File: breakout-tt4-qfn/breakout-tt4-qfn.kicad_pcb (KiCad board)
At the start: 2 copper layers, 45 x 52.5 mm, 113 parts, among them U1 Caravel_QFN_TT4

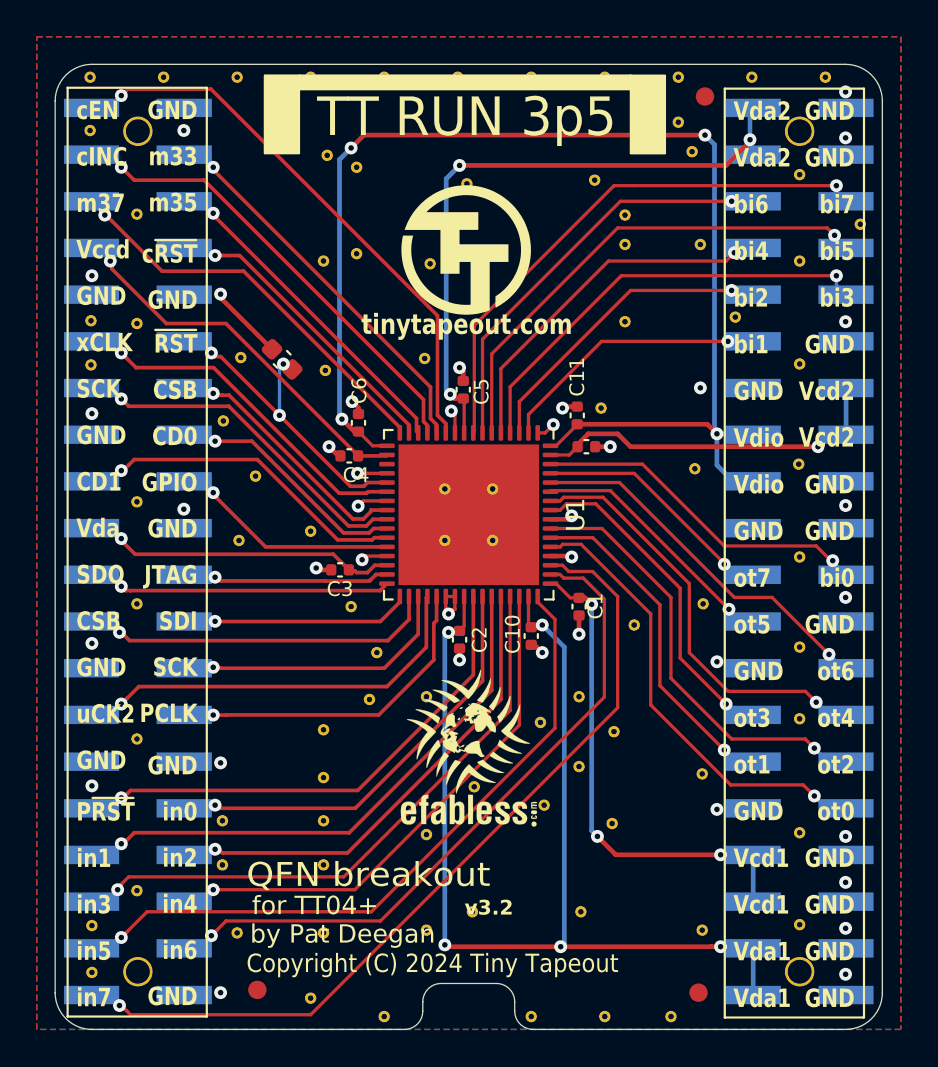
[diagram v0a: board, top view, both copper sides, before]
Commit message: modified silk for TT04
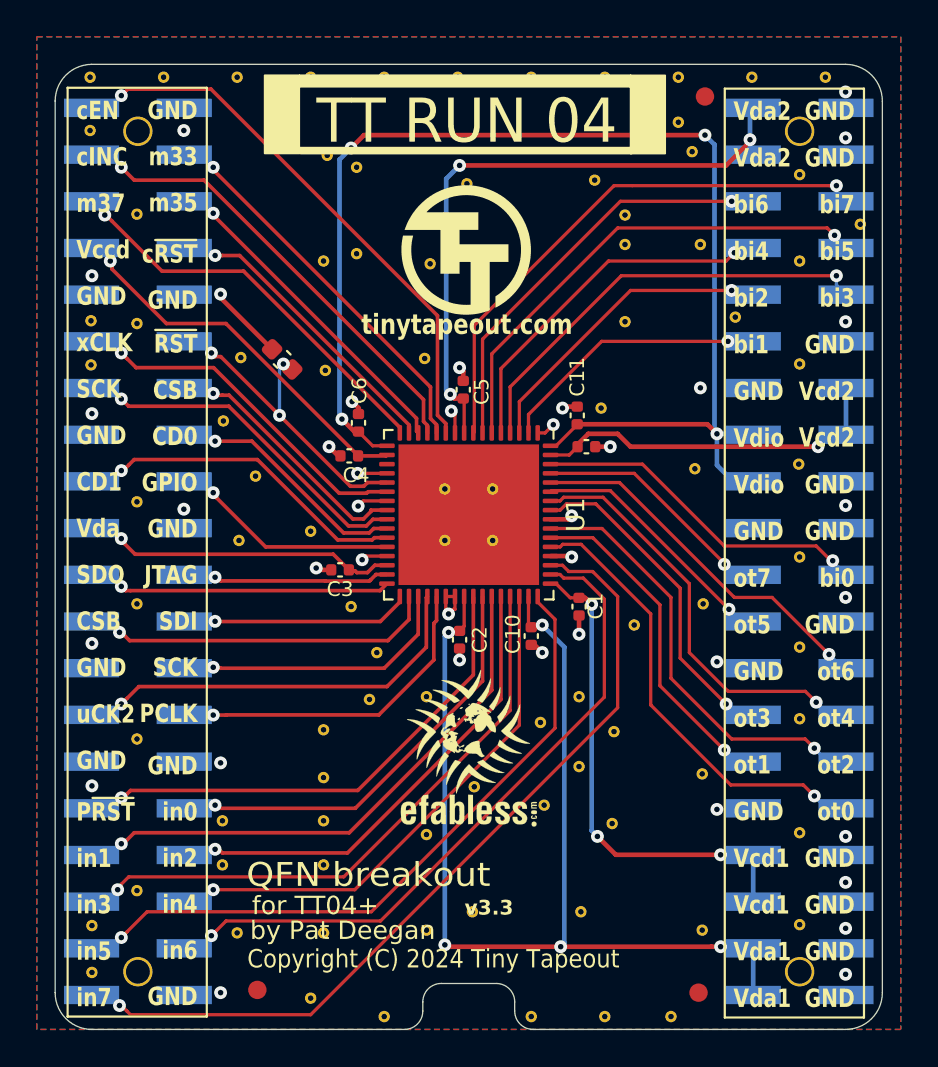
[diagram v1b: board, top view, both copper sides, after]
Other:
- board text added: "Design by Pat Deegan https://psychogenic.com"
- board text added: "TT RUN 04"
- board text added: "TinyTapeout designs are packaged together along with a MUX that allows for directing I/O to any selected project, controlled through the cINC, cEN and ~{cRST} pins. This PCB provides a way to deliver these chips that will sit atop the demo board, but also allows you to easily integrate the ICs into your own projects. For details, see"
- board text added: "github.com/TinyTapeout/breakout-pcb"
- board text added: "v3.3"
- board text removed: "TT RUN 3p5"
- board text removed: "TinyTapeout projects are packaged together within Caravel, an SoC that provides space for user projects, pads to connect to the outside world and other features like a microcontroller, logic analyzer, etc. This PCB provides a way to deliver these chips that will sit atop the demo board, but also allows you to easily integrate the ICs into your own projects. For details, see"
- board text removed: "by Pat Deegan https://psychogenic.com"
- board text removed: "github.com/TinyTapeout/caravel-breakout-pcb"
- board text removed: "v3.2"
